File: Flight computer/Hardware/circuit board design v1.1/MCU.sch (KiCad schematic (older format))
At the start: 30 parts, among them J1 Conn_01x05, U11 W25Q64JVSSIM, U7 ATSAMD21J18A-AU, Y3 16MHz

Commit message: Fully routed board v1.1 with the new high g accelerometer
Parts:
- C86, C88: footprint Capacitor_SMD:C_0402_1005Metric -> Capacitor_SMD:C_0603_1608Metric
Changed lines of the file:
@@
 F 0 "C88" H 3865 4696 50  0000 L CNN
 F 1 "15pF" H 3865 4605 50  0000 L CNN
-F 2 "Capacitor_SMD:C_0402_1005Metric" H 3788 4500 50  0001 C CNN
+F 2 "Capacitor_SMD:C_0603_1608Metric" H 3788 4500 50  0001 C CNN
 F 3 "~" H 3750 4650 50  0001 C CNN
 	1    3750 4650
@@
 F 0 "C86" H 2915 4696 50  0000 L CNN
 F 1 "15pF" H 2915 4605 50  0000 L CNN
-F 2 "Capacitor_SMD:C_0402_1005Metric" H 2838 4500 50  0001 C CNN
+F 2 "Capacitor_SMD:C_0603_1608Metric" H 2838 4500 50  0001 C CNN
 F 3 "~" H 2800 4650 50  0001 C CNN
 	1    2800 4650

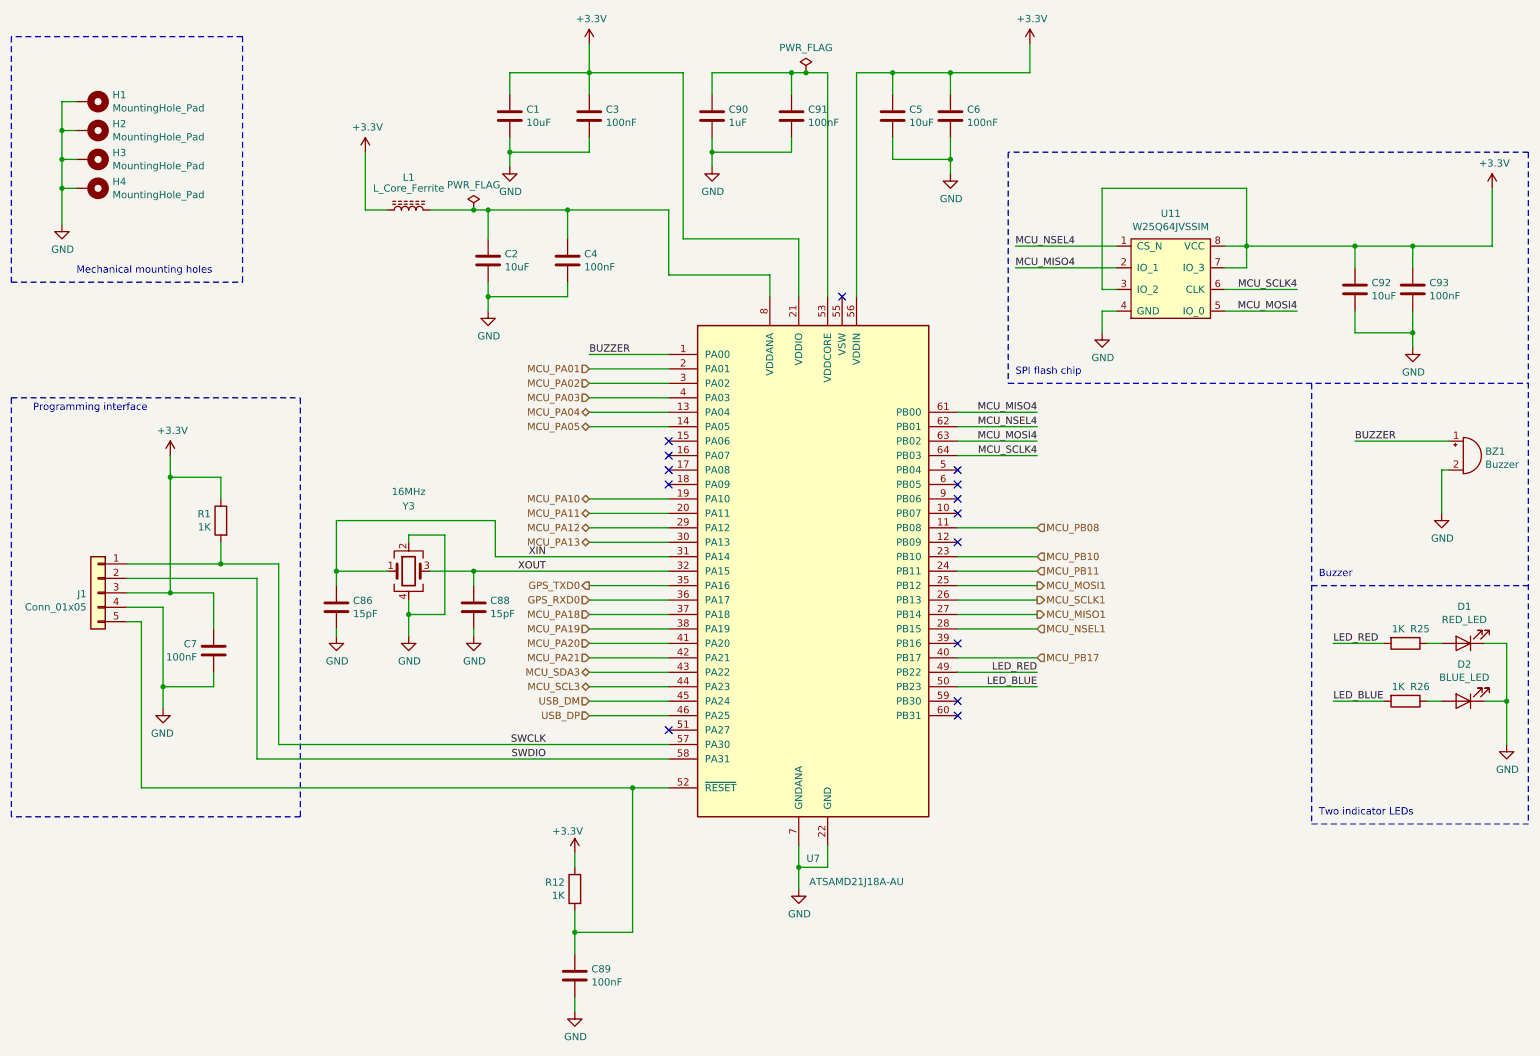
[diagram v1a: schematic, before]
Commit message: put in logo for V1.1
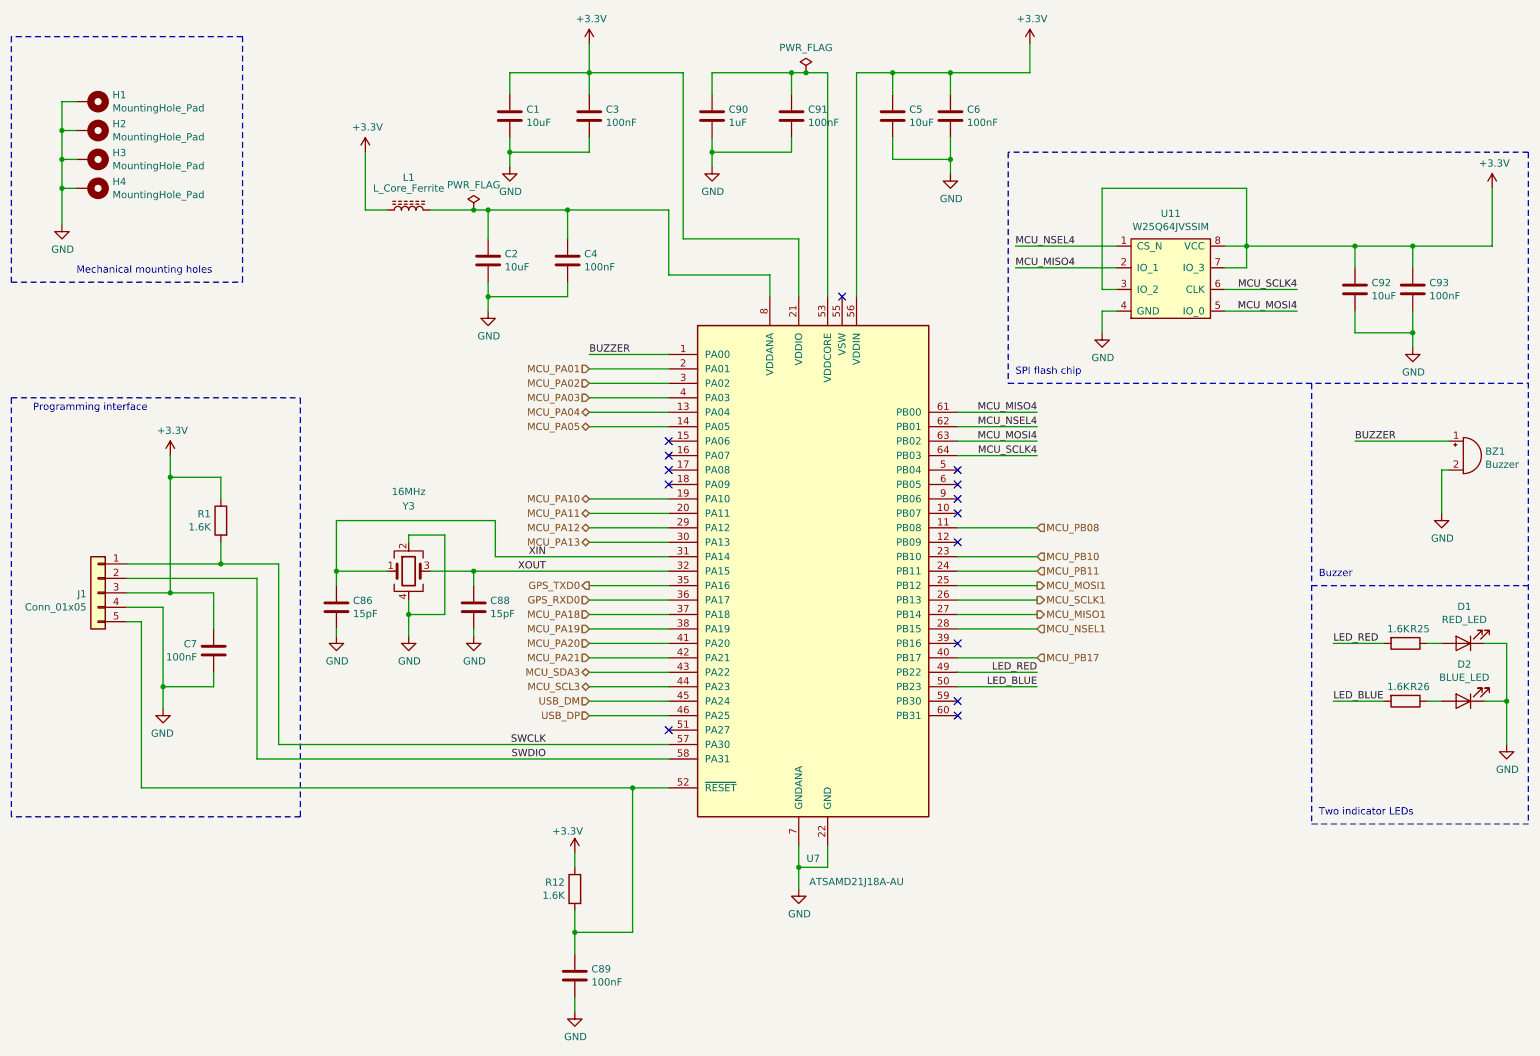
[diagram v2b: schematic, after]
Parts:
- C1, C2, C5, C92: Cost (none) -> 0.07; Purchase link (none) -> https://uk.rs-online.com/web/p/mlccs-multilayer-ceramic-cap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; min_quantity (none) -> 100
- C3, C4, C6, C7, C89, C91, C93: Cost (none) -> 0.01; Purchase link (none) -> https://uk.rs-online.com/web/p/mlccs-multilayer-ceramic-cap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; min_quantity (none) -> 50
- C90: Cost (none) -> 0.01; Purchase link (none) -> https://uk.rs-online.com/web/p/mlccs-multilayer-ceramic-cap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; min_quantity (none) -> 250
- H1, H2, H3, H4: Cost (none) -> 0.0
- L1: Cost (none) -> 0.05; Purchase link (none) -> https://uk.rs-online.com/web/p/ferrite-beads/7926299/; min_quantity (none) -> 25
- R1, R12, R25, R26: value 1K -> 1.6K; Cost (none) -> 0.002; Purchase link (none) -> https://uk.rs-online.com/web/p/surface-mount-fixed-resistor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; min_quantity (none) -> 50
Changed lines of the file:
@@
 P 4450 6600
 F 0 "R12" H 4520 6646 50  0000 L CNN
-F 1 "1K" H 4520 6555 50  0000 L CNN
+F 1 "1.6K" H 4520 6555 50  0000 L CNN
 F 2 "Resistor_SMD:R_0603_1608Metric" V 4380 6600 50  0001 C CNN
 F 3 "~" H 4450 6600 50  0001 C CNN
+F 4 "0.002" H 4450 6600 50  0001 C CNN "Cost"
+F 5 "https://uk.rs-online.com/web/p/surface-mount-fixed-resistors/6789917/" H 4450 6600 50  0001 C CNN "Purchase link"
+F 6 "50" H 4450 6600 50  0001 C CNN "min_quantity"
 	1    4450 6600
 	-1   0    0    -1
@@
 F 2 "MountingHole:MountingHole_3.2mm_M3_Pad" H 1100 1750 50  0001 C CNN
 F 3 "~" H 1100 1750 50  0001 C CNN
+F 4 "0.0" H 1100 1750 50  0001 C CNN "Cost"
 	1    1100 1750
 	0    1    1    0
@@
 F 2 "MountingHole:MountingHole_3.2mm_M3_Pad" H 1100 1550 50  0001 C CNN
 F 3 "~" H 1100 1550 50  0001 C CNN
+F 4 "0.0" H 1100 1550 50  0001 C CNN "Cost"
 	1    1100 1550
 	0    1    1    0
@@
 F 2 "MountingHole:MountingHole_3.2mm_M3_Pad" H 1100 1350 50  0001 C CNN
 F 3 "~" H 1100 1350 50  0001 C CNN
+F 4 "0.0" H 1100 1350 50  0001 C CNN "Cost"
 	1    1100 1350
 	0    1    1    0
@@
 F 2 "MountingHole:MountingHole_3.2mm_M3_Pad" H 1100 1150 50  0001 C CNN
 F 3 "~" H 1100 1150 50  0001 C CNN
+F 4 "0.0" H 1100 1150 50  0001 C CNN "Cost"
 	1    1100 1150
 	0    1    1    0
@@
 P 10200 4900
 F 0 "R25" V 10100 5000 50  0000 C CNN
-F 1 "1K" V 10100 4850 50  0000 C CNN
+F 1 "1.6K" V 10100 4850 50  0000 C CNN
 F 2 "Resistor_SMD:R_0603_1608Metric" V 10130 4900 50  0001 C CNN
 F 3 "~" H 10200 4900 50  0001 C CNN
+F 4 "0.002" H 10200 4900 50  0001 C CNN "Cost"
+F 5 "https://uk.rs-online.com/web/p/surface-mount-fixed-resistors/6789917/" H 10200 4900 50  0001 C CNN "Purchase link"
+F 6 "50" H 10200 4900 50  0001 C CNN "min_quantity"
 	1    10200 4900
 	0    1    1    0
@@
 P 10200 5300
 F 0 "R26" V 10100 5400 50  0000 C CNN
-F 1 "1K" V 10100 5250 50  0000 C CNN
+F 1 "1.6K" V 10100 5250 50  0000 C CNN
 F 2 "Resistor_SMD:R_0603_1608Metric" V 10130 5300 50  0001 C CNN
 F 3 "~" H 10200 5300 50  0001 C CNN
+F 4 "0.002" H 10200 5300 50  0001 C CNN "Cost"
+F 5 "https://uk.rs-online.com/web/p/surface-mount-fixed-resistors/6789917/" H 10200 5300 50  0001 C CNN "Purchase link"
+F 6 "50" H 10200 5300 50  0001 C CNN "min_quantity"
 	1    10200 5300
 	0    1    1    0
@@
 F 1 "L_Core_Ferrite" V 3450 1900 50  0000 C CNN
 F 2 "Inductor_SMD:L_0603_1608Metric" H 3300 1900 50  0001 C CNN
-F 3 "~" H 3300 1900 50  0001 C CNN
+F 3 "https://docs-emea.rs-online.com/webdocs/07a1/0900766b807a1caf.pdf" H 3300 1900 50  0001 C CNN
+F 4 "0.05" H 3300 1900 50  0001 C CNN "Cost"
+F 5 "https://uk.rs-online.com/web/p/ferrite-beads/7926299/" H 3300 1900 50  0001 C CNN "Purchase link"
+F 6 "25" H 3300 1900 50  0001 C CNN "min_quantity"
 	1    3300 1900
 	0    -1   -1   0
@@
 F 1 "100nF" H 4565 7155 50  0000 L CNN
 F 2 "Capacitor_SMD:C_0603_1608Metric" H 4488 7050 50  0001 C CNN
-F 3 "~" H 4450 7200 50  0001 C CNN
+F 3 "https://docs-emea.rs-online.com/webdocs/0dc2/0900766b80dc2409.pdf" H 4450 7200 50  0001 C CNN
+F 4 "0.01" H 4450 7200 50  0001 C CNN "Cost"
+F 5 "https://uk.rs-online.com/web/p/mlccs-multilayer-ceramic-capacitors/6983251/" H 4450 7200 50  0001 C CNN "Purchase link"
+F 6 "50" H 4450 7200 50  0001 C CNN "min_quantity"
 	1    4450 7200
 	1    0    0    -1
@@
 F 2 "Capacitor_SMD:C_0603_1608Metric" H 5438 1100 50  0001 C CNN
 F 3 "~" H 5400 1250 50  0001 C CNN
+F 4 "0.01" H 5400 1250 50  0001 C CNN "Cost"
+F 5 "https://uk.rs-online.com/web/p/mlccs-multilayer-ceramic-capacitors/1358359/" H 5400 1250 50  0001 C CNN "Purchase link"
+F 6 "250" H 5400 1250 50  0001 C CNN "min_quantity"
 	1    5400 1250
 	1    0    0    -1
@@
 F 1 "100nF" H 6065 1205 50  0000 L CNN
 F 2 "Capacitor_SMD:C_0603_1608Metric" H 5988 1100 50  0001 C CNN
-F 3 "~" H 5950 1250 50  0001 C CNN
+F 3 "https://docs-emea.rs-online.com/webdocs/0dc2/0900766b80dc2409.pdf" H 5950 1250 50  0001 C CNN
+F 4 "0.01" H 5950 1250 50  0001 C CNN "Cost"
+F 5 "https://uk.rs-online.com/web/p/mlccs-multilayer-ceramic-capacitors/6983251/" H 5950 1250 50  0001 C CNN "Purchase link"
+F 6 "50" H 5950 1250 50  0001 C CNN "min_quantity"
 	1    5950 1250
 	1    0    0    -1
@@
 F 1 "10uF" H 9965 2405 50  0000 L CNN
 F 2 "Capacitor_SMD:C_0603_1608Metric" H 9888 2300 50  0001 C CNN
-F 3 "~" H 9850 2450 50  0001 C CNN
+F 3 "https://docs-emea.rs-online.com/webdocs/13b3/0900766b813b3e64.pdf" H 9850 2450 50  0001 C CNN
+F 4 "0.07" H 9850 2450 50  0001 C CNN "Cost"
+F 5 "https://uk.rs-online.com/web/p/mlccs-multilayer-ceramic-capacitors/8467293/" H 9850 2450 50  0001 C CNN "Purchase link"
+F 6 "100" H 9850 2450 50  0001 C CNN "min_quantity"
 	1    9850 2450
 	1    0    0    -1
@@
 F 1 "100nF" H 10365 2405 50  0000 L CNN
 F 2 "Capacitor_SMD:C_0603_1608Metric" H 10288 2300 50  0001 C CNN
-F 3 "~" H 10250 2450 50  0001 C CNN
+F 3 "https://docs-emea.rs-online.com/webdocs/0dc2/0900766b80dc2409.pdf" H 10250 2450 50  0001 C CNN
+F 4 "0.01" H 10250 2450 50  0001 C CNN "Cost"
+F 5 "https://uk.rs-online.com/web/p/mlccs-multilayer-ceramic-capacitors/6983251/" H 10250 2450 50  0001 C CNN "Purchase link"
+F 6 "50" H 10250 2450 50  0001 C CNN "min_quantity"
 	1    10250 2450
 	1    0    0    -1
@@
 F 1 "10uF" H 6765 1205 50  0000 L CNN
 F 2 "Capacitor_SMD:C_0603_1608Metric" H 6688 1100 50  0001 C CNN
-F 3 "~" H 6650 1250 50  0001 C CNN
+F 3 "https://docs-emea.rs-online.com/webdocs/13b3/0900766b813b3e64.pdf" H 6650 1250 50  0001 C CNN
+F 4 "0.07" H 6650 1250 50  0001 C CNN "Cost"
+F 5 "https://uk.rs-online.com/web/p/mlccs-multilayer-ceramic-capacitors/8467293/" H 6650 1250 50  0001 C CNN "Purchase link"
+F 6 "100" H 6650 1250 50  0001 C CNN "min_quantity"
 	1    6650 1250
 	1    0    0    -1
@@
 F 1 "100nF" H 7165 1205 50  0000 L CNN
 F 2 "Capacitor_SMD:C_0603_1608Metric" H 7088 1100 50  0001 C CNN
-F 3 "~" H 7050 1250 50  0001 C CNN
+F 3 "https://docs-emea.rs-online.com/webdocs/0dc2/0900766b80dc2409.pdf" H 7050 1250 50  0001 C CNN
+F 4 "0.01" H 7050 1250 50  0001 C CNN "Cost"
+F 5 "https://uk.rs-online.com/web/p/mlccs-multilayer-ceramic-capacitors/6983251/" H 7050 1250 50  0001 C CNN "Purchase link"
+F 6 "50" H 7050 1250 50  0001 C CNN "min_quantity"
 	1    7050 1250
 	1    0    0    -1
@@
 F 1 "100nF" H 2065 4905 50  0000 L CNN
 F 2 "Capacitor_SMD:C_0603_1608Metric" H 1988 4800 50  0001 C CNN
-F 3 "~" H 1950 4950 50  0001 C CNN
+F 3 "https://docs-emea.rs-online.com/webdocs/0dc2/0900766b80dc2409.pdf" H 1950 4950 50  0001 C CNN
+F 4 "0.01" H 1950 4950 50  0001 C CNN "Cost"
+F 5 "https://uk.rs-online.com/web/p/mlccs-multilayer-ceramic-capacitors/6983251/" H 1950 4950 50  0001 C CNN "Purchase link"
+F 6 "50" H 1950 4950 50  0001 C CNN "min_quantity"
 	1    1950 4950
 	-1   0    0    -1
@@
 P 2000 4050
 F 0 "R1" H 2070 4096 50  0000 L CNN
-F 1 "1K" H 2070 4005 50  0000 L CNN
+F 1 "1.6K" H 2070 4005 50  0000 L CNN
 F 2 "Resistor_SMD:R_0603_1608Metric" V 1930 4050 50  0001 C CNN
 F 3 "~" H 2000 4050 50  0001 C CNN
+F 4 "0.002" H 2000 4050 50  0001 C CNN "Cost"
+F 5 "https://uk.rs-online.com/web/p/surface-mount-fixed-resistors/6789917/" H 2000 4050 50  0001 C CNN "Purchase link"
+F 6 "50" H 2000 4050 50  0001 C CNN "min_quantity"
 	1    2000 4050
 	-1   0    0    -1
@@
 F 1 "10uF" H 4115 1205 50  0000 L CNN
 F 2 "Capacitor_SMD:C_0603_1608Metric" H 4038 1100 50  0001 C CNN
-F 3 "~" H 4000 1250 50  0001 C CNN
+F 3 "https://docs-emea.rs-online.com/webdocs/13b3/0900766b813b3e64.pdf" H 4000 1250 50  0001 C CNN
+F 4 "0.07" H 4000 1250 50  0001 C CNN "Cost"
+F 5 "https://uk.rs-online.com/web/p/mlccs-multilayer-ceramic-capacitors/8467293/" H 4000 1250 50  0001 C CNN "Purchase link"
+F 6 "100" H 4000 1250 50  0001 C CNN "min_quantity"
 	1    4000 1250
 	1    0    0    -1
@@
 F 1 "100nF" H 4665 1205 50  0000 L CNN
 F 2 "Capacitor_SMD:C_0603_1608Metric" H 4588 1100 50  0001 C CNN
-F 3 "~" H 4550 1250 50  0001 C CNN
+F 3 "https://docs-emea.rs-online.com/webdocs/0dc2/0900766b80dc2409.pdf" H 4550 1250 50  0001 C CNN
+F 4 "0.01" H 4550 1250 50  0001 C CNN "Cost"
+F 5 "https://uk.rs-online.com/web/p/mlccs-multilayer-ceramic-capacitors/6983251/" H 4550 1250 50  0001 C CNN "Purchase link"
+F 6 "50" H 4550 1250 50  0001 C CNN "min_quantity"
 	1    4550 1250
 	1    0    0    -1
@@
 F 1 "10uF" H 3965 2205 50  0000 L CNN
 F 2 "Capacitor_SMD:C_0603_1608Metric" H 3888 2100 50  0001 C CNN
-F 3 "~" H 3850 2250 50  0001 C CNN
+F 3 "https://docs-emea.rs-online.com/webdocs/13b3/0900766b813b3e64.pdf" H 3850 2250 50  0001 C CNN
+F 4 "0.07" H 3850 2250 50  0001 C CNN "Cost"
+F 5 "https://uk.rs-online.com/web/p/mlccs-multilayer-ceramic-capacitors/8467293/" H 3850 2250 50  0001 C CNN "Purchase link"
+F 6 "100" H 3850 2250 50  0001 C CNN "min_quantity"
 	1    3850 2250
 	1    0    0    -1
@@
 F 1 "100nF" H 4515 2205 50  0000 L CNN
 F 2 "Capacitor_SMD:C_0603_1608Metric" H 4438 2100 50  0001 C CNN
-F 3 "~" H 4400 2250 50  0001 C CNN
+F 3 "https://docs-emea.rs-online.com/webdocs/0dc2/0900766b80dc2409.pdf" H 4400 2250 50  0001 C CNN
+F 4 "0.01" H 4400 2250 50  0001 C CNN "Cost"
+F 5 "https://uk.rs-online.com/web/p/mlccs-multilayer-ceramic-capacitors/6983251/" H 4400 2250 50  0001 C CNN "Purchase link"
+F 6 "50" H 4400 2250 50  0001 C CNN "min_quantity"
 	1    4400 2250
 	1    0    0    -1

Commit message: changed GPS to M8Q and included the diode from V bus to foot print which I missed out
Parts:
- C86, C88: Cost (none) -> 0.043; Purchase link (none) -> https://uk.rs-online.com/web/p/mlccs-multilayer-ceramic-cap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; min_quantity (none) -> 25
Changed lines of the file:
@@
 F 2 "Capacitor_SMD:C_0603_1608Metric" H 3788 4500 50  0001 C CNN
 F 3 "~" H 3750 4650 50  0001 C CNN
+F 4 "0.043" H 3750 4650 50  0001 C CNN "Cost"
+F 5 "https://uk.rs-online.com/web/p/mlccs-multilayer-ceramic-capacitors/3936659/" H 3750 4650 50  0001 C CNN "Purchase link"
+F 6 "25" H 3750 4650 50  0001 C CNN "min_quantity"
 	1    3750 4650
 	1    0    0    -1
@@
 F 2 "Capacitor_SMD:C_0603_1608Metric" H 2838 4500 50  0001 C CNN
 F 3 "~" H 2800 4650 50  0001 C CNN
+F 4 "0.043" H 2800 4650 50  0001 C CNN "Cost"
+F 5 "https://uk.rs-online.com/web/p/mlccs-multilayer-ceramic-capacitors/3936659/" H 2800 4650 50  0001 C CNN "Purchase link"
+F 6 "25" H 2800 4650 50  0001 C CNN "min_quantity"
 	1    2800 4650
 	1    0    0    -1
